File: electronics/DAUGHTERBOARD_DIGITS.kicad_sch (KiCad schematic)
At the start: 14 parts, among them Q2 AO3400A, Q3 AO3400A, U4 HDSM-443B, U5 74HC157, U6 HEF4543B, U7 74LVC1GU04DRL, U8 74HC595, U9 74LVC1GU04DRL

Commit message: Addon modifications
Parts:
- added C11, C12, C2: 100n, Capacitor_SMD:C_0603_1608Metric, symbol Device:C
- RN1, RN2: value R_Pack04 -> 120
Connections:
- net +3V3: now also U5.16 (VCC), U8.10 (~{SRCLR}), U8.16 (VCC), C11.1, C12.1, C2.1
- net GND: now also C11.2, C12.2, C2.2
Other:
- note added: "one decoupling cap 100n 0603 for each chip, including inverters u6 also gets a 1u decoupling"
- note removed: "one decoupling cap 100n 0603 for each chip, including inverters"
- moved on the sheet: C1, Q2, Q3, R1, R2, R3, RN1, RN2, U4, U5, U6, U7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

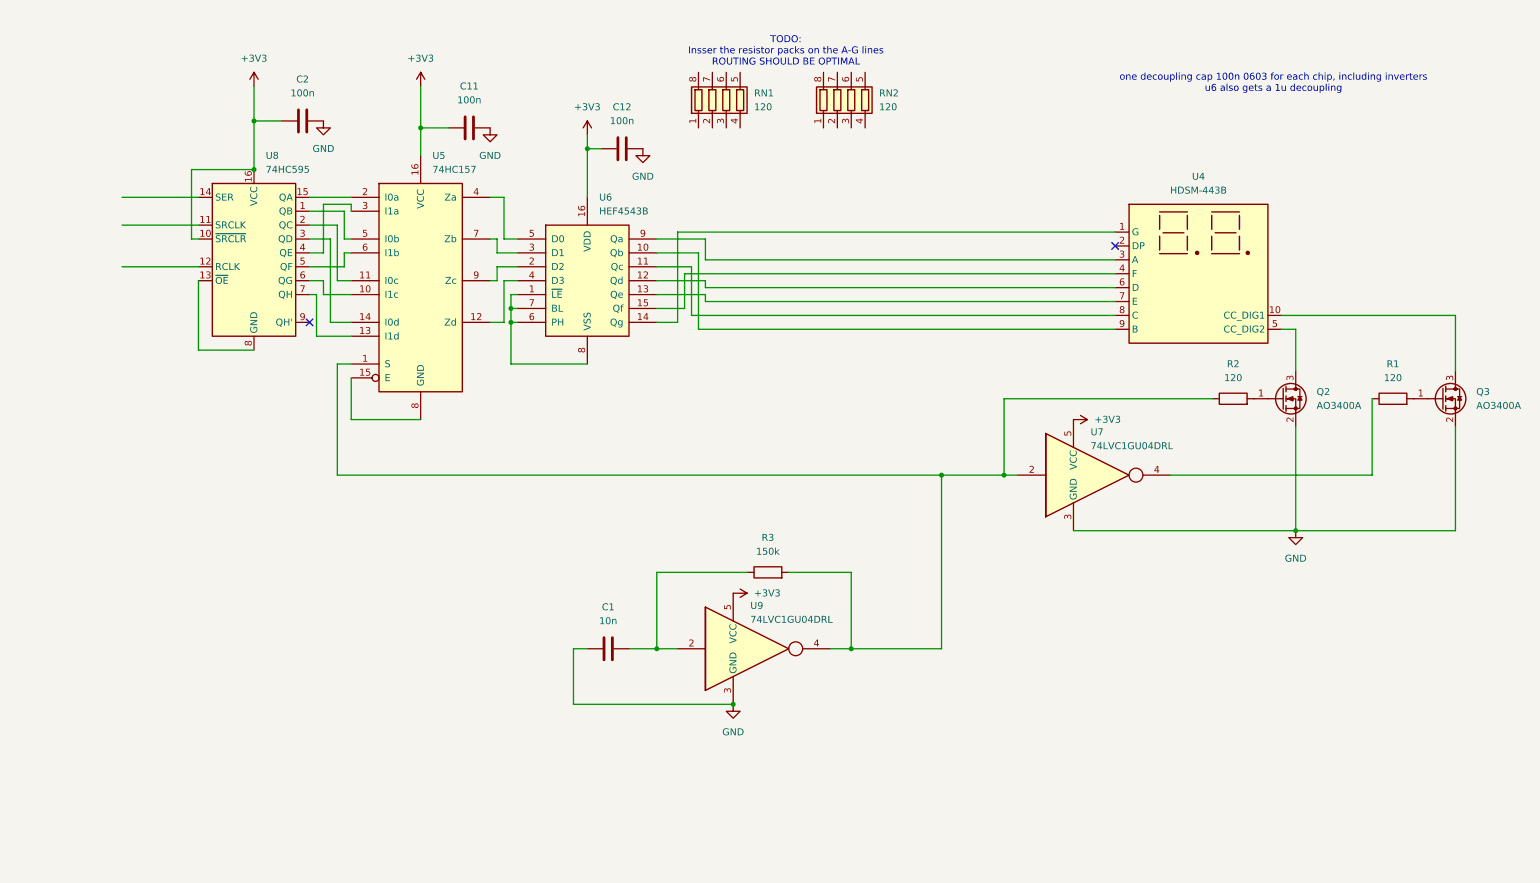
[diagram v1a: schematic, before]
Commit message: Rework scematic for addon
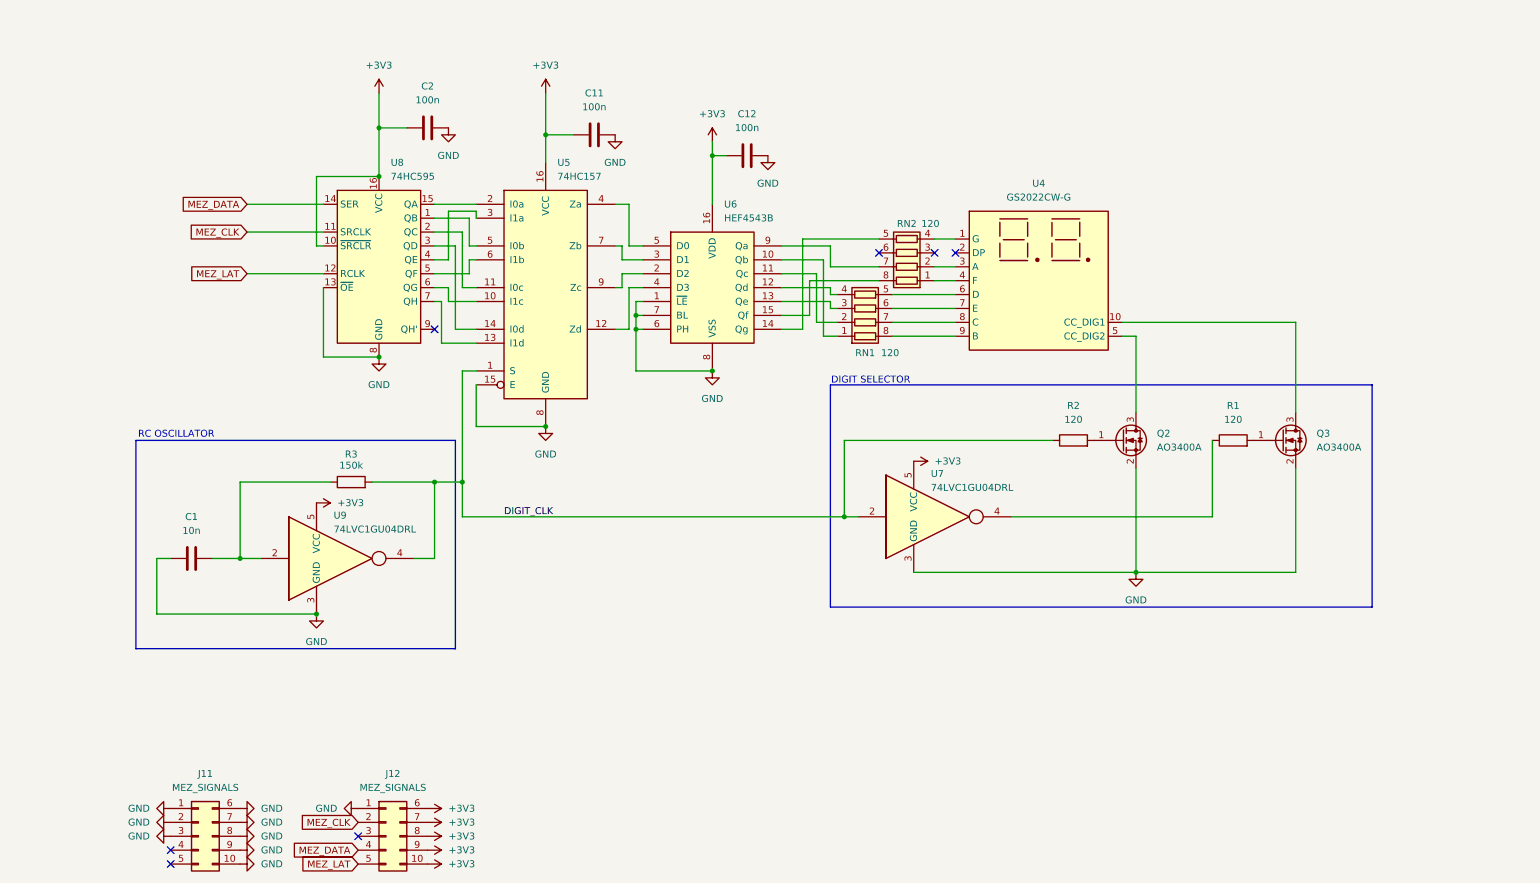
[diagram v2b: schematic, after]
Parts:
- added J11, J12: MEZ_SIGNALS, Connector_Hirose:Hirose_DF12_DF12E3.0-10DP-0.5V_2x05_P0.50mm_Vertical, symbol Connector_Generic:Conn_02x05_Top_Bottom
- C1: footprint (none) -> Capacitor_SMD:C_0603_1608Metric
- R3: footprint (none) -> Resistor_SMD:R_0603_1608Metric
- U4: value HDSM-443B -> GS2022CW-G; LCSC (none) -> C27636668
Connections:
- net +3V3: now also J12.10 (Pin_10), J12.6 (Pin_6), J12.7 (Pin_7), J12.8 (Pin_8), J12.9 (Pin_9)
- net GND: now also U5.15 (E), U5.8 (GND), U6.1 (~{LE}), U6.6 (PH), U6.7 (BL), U6.8 (VSS), U8.13 (~{OE}), U8.8 (GND), J11.1 (Pin_1), J11.10 (Pin_10), J11.2 (Pin_2), J11.3 (Pin_3), J11.6 (Pin_6), J11.7 (Pin_7), J11.8 (Pin_8), J11.9 (Pin_9), J12.1 (Pin_1)
- net DIGIT_CLK: now reaches R2.1, R3.2, U5.1 (S), U7.2, U9.4
- net at RN1.1 (R1.1): now also U6.10 (Qb)
- net at RN1.2 (R2.1): now also U6.11 (Qc)
- net at RN1.3 (R3.1): now also U6.13 (Qe)
- net at RN1.4 (R4.1): now also U6.12 (Qd)
- net at RN1.5 (R4.2): now also U4.6 (D)
- net at RN1.6 (R3.2): now also U4.7 (E)
- net at RN1.7 (R2.2): now also U4.8 (C)
- net at RN1.8 (R1.2): now also U4.9 (B)
- net at U4.1 (G): now also RN2.4 (R4.1); no longer U6.14 (Qg)
- net at U4.3 (A): now also RN2.2 (R2.1); no longer U6.9 (Qa)
- net at U4.4 (F): now also RN2.1 (R1.1); no longer U6.15 (Qf)
- net at RN2.5 (R4.2): now also U6.14 (Qg)
- net at RN2.7 (R2.2): now also U6.9 (Qa)
- net at RN2.8 (R1.2): now also U6.15 (Qf)
- net MEZ_CLK: now reaches U8.11 (SRCLK)
- net MEZ_CLK: now also J12.2 (Pin_2)
- net MEZ_LAT: now reaches U8.12 (RCLK)
- net MEZ_LAT: now also J12.5 (Pin_5)
- net MEZ_DATA: now reaches U8.14 (SER)
- net MEZ_DATA: now also J12.4 (Pin_4)
- no-connect marks 2 -> 7
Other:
- note added: "DIGIT SELECTOR"
- note added: "RC OSCILLATOR"
- note removed: "TODO: Insser the resistor packs on the A-G lines ROUTING SHOULD BE OPTIMAL"
- note removed: "one decoupling cap 100n 0603 for each chip, including inverters u6 also gets a 1u decoupling"
- moved on the sheet: C1, C11, C12, C2, Q2, Q3, R1, R2, R3, RN1, RN2, U4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
